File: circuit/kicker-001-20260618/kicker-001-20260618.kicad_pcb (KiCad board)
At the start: 2 copper layers, 71.4 x 62.3 mm, 0 parts

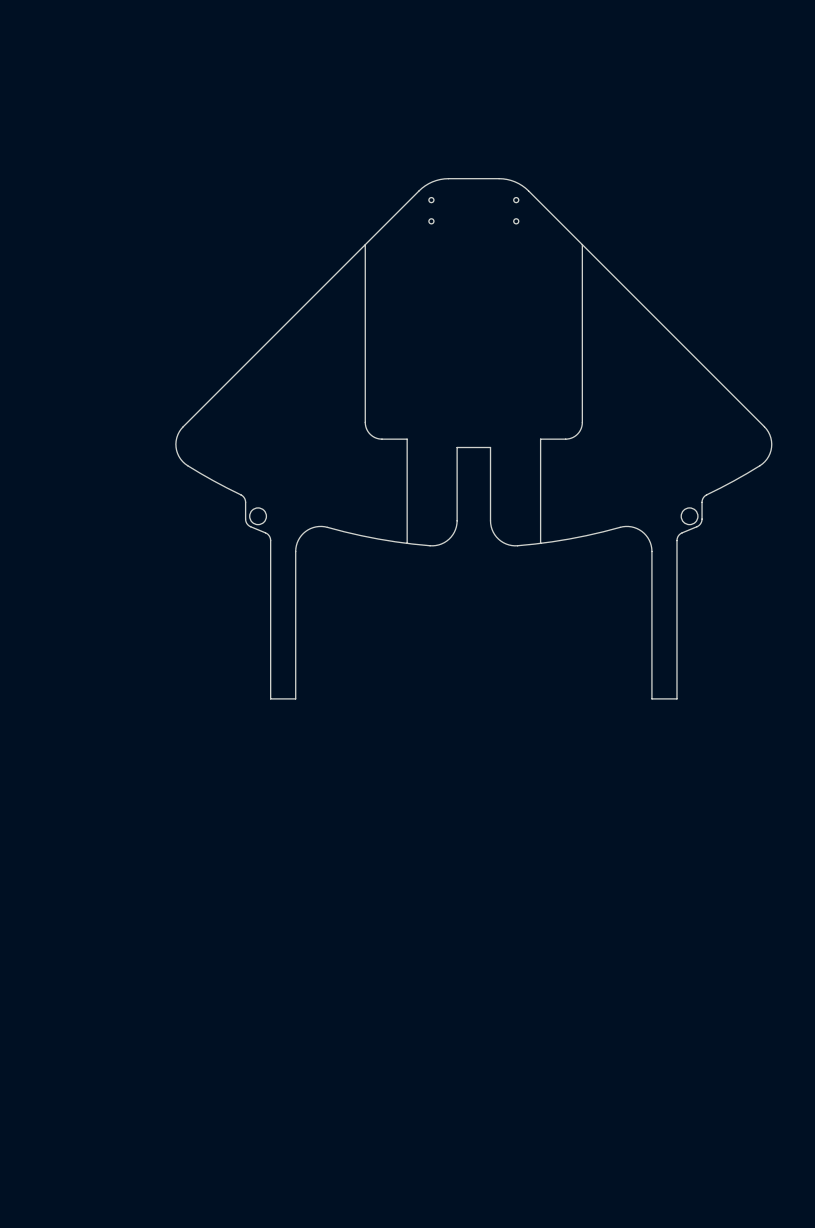
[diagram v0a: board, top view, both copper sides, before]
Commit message: Update キッカー基板のボード図を更新した
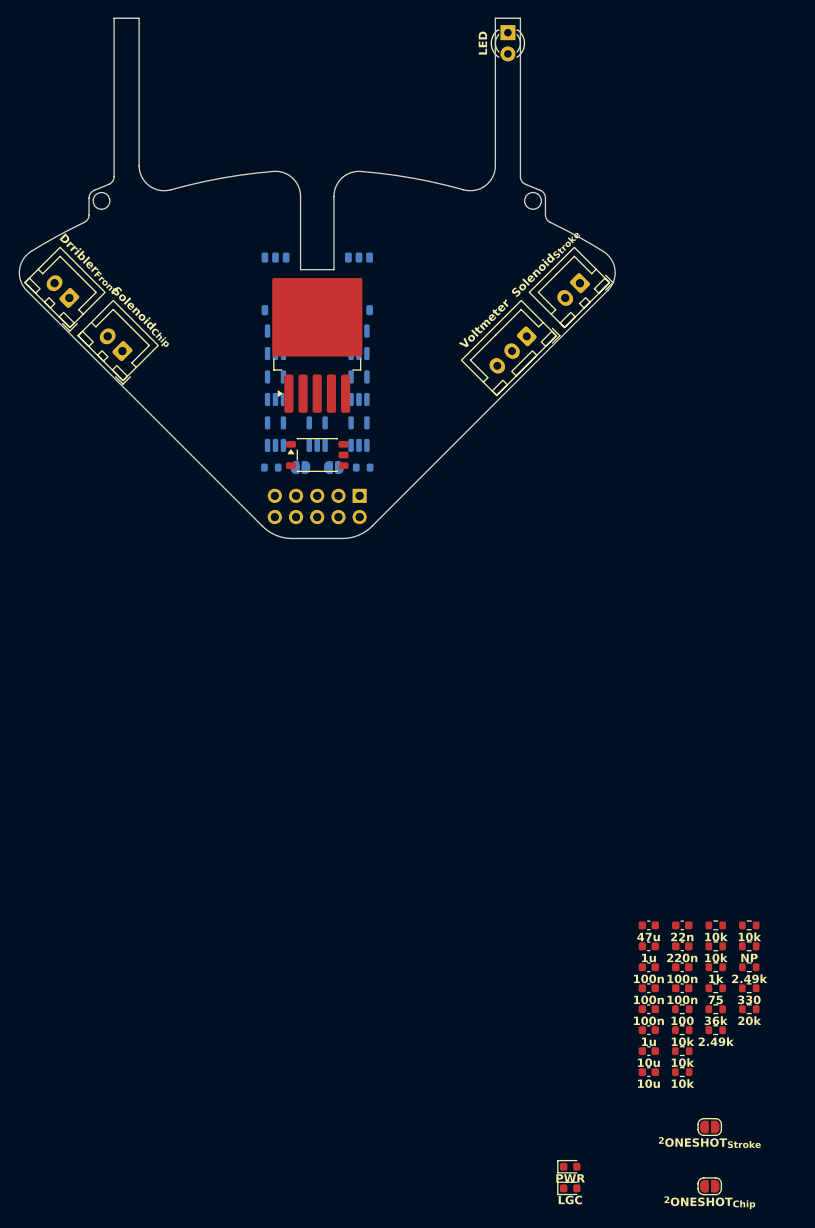
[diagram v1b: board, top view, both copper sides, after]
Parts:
- added C1: 47u, Capacitor_SMD:C_0603_1608Metric, F.Cu at (139.7, 146.3)
- added C10: 220n, Capacitor_SMD:C_0603_1608Metric, F.Cu at (143.7, 148.8)
- added C11: 100n, Capacitor_SMD:C_0603_1608Metric, F.Cu at (143.7, 151.4)
- added C12: 100n, Capacitor_SMD:C_0603_1608Metric, F.Cu at (143.7, 153.9)
- added C2: 1u, Capacitor_SMD:C_0603_1608Metric, F.Cu at (139.7, 148.8)
- added C3: 100n, Capacitor_SMD:C_0603_1608Metric, F.Cu at (139.7, 151.4)
- added C4: 100n, Capacitor_SMD:C_0603_1608Metric, F.Cu at (139.7, 153.9)
- added C5: 100n, Capacitor_SMD:C_0603_1608Metric, F.Cu at (139.7, 156.4)
- added C6: 1u, Capacitor_SMD:C_0603_1608Metric, F.Cu at (139.7, 158.9)
- added C7: 10u, Capacitor_SMD:C_0603_1608Metric, F.Cu at (139.7, 161.4)
- added C8: 10u, Capacitor_SMD:C_0603_1608Metric, F.Cu at (139.7, 163.9)
- added C9: 22n, Capacitor_SMD:C_0603_1608Metric, F.Cu at (143.7, 146.3)
- added D1: LED, LED_THT:LED_D3.0mm, F.Cu at (122.8, 39.4)
- added D3: PWR, LED_SMD:LED_0603_1608Metric, F.Cu at (130.3, 175.2)
- added D4: LGC, LED_SMD:LED_0603_1608Metric, F.Cu at (130.3, 177.8)
- added J1: Solenoid_{Stroke}, Connector_JST:JST_XH_B2B-XH-A_1x02_P2.50mm_Vertical, F.Cu at (131.5, 69.4)
- added J2: Solenoid_{Chip}, Connector_JST:JST_XH_B2B-XH-A_1x02_P2.50mm_Vertical, F.Cu at (76.7, 77.6)
- added J3: Drribler_{Front}, Connector_JST:JST_XH_B2B-XH-A_1x02_P2.50mm_Vertical, F.Cu at (70.3, 71.2)
- added J4: Conn_Relay, Connector_PinSocket_2.54mm:PinSocket_2x05_P2.54mm_Vertical, B.Cu at (105.1, 94.9)
- added J5: Voltmeter, Connector_JST:JST_XH_B3B-XH-A_1x03_P2.50mm_Vertical, F.Cu at (125.1, 75.8)
- added JP1: ^{1}ONESHOT_{Stroke}, Jumper:SolderJumper-2_P1.3mm_Open_RoundedPad1.0x1.5mm, B.Cu at (98.0, 91.5)
- added JP2: ^{2}ONESHOT_{Stroke}, Jumper:SolderJumper-2_P1.3mm_Open_RoundedPad1.0x1.5mm, F.Cu at (147.0, 170.5)
- added JP3: ^{1}ONESHOT_{Chip}, Jumper:SolderJumper-2_P1.3mm_Open_RoundedPad1.0x1.5mm, B.Cu at (102.0, 91.5)
- added JP4: ^{2}ONESHOT_{Chip}, Jumper:SolderJumper-2_P1.3mm_Open_RoundedPad1.0x1.5mm, F.Cu at (147.0, 177.6)
- added R1: 100, Resistor_SMD:R_0603_1608Metric, F.Cu at (143.7, 156.4)
- added R10: 2.49k, Resistor_SMD:R_0603_1608Metric, F.Cu at (147.7, 158.9)
- added R11: 100k, Resistor_SMD:R_0603_1608Metric, B.Cu at (94.5, 91.5)
- added R12: 100k, Resistor_SMD:R_0603_1608Metric, B.Cu at (105.5, 91.5)
- added R13: 10k, Resistor_SMD:R_0603_1608Metric, F.Cu at (151.7, 146.3)
- added R14: NP, Resistor_SMD:R_0603_1608Metric, F.Cu at (151.7, 148.8)
- added R15: 2.49k, Resistor_SMD:R_0603_1608Metric, F.Cu at (151.7, 151.4)
- added R16: 330, Resistor_SMD:R_0603_1608Metric, F.Cu at (151.7, 153.9)
- added R17: 20k, Resistor_SMD:R_0603_1608Metric, F.Cu at (151.7, 156.4)
- added R2: 10k, Resistor_SMD:R_0603_1608Metric, F.Cu at (143.7, 158.9)
- added R3: 10k, Resistor_SMD:R_0603_1608Metric, F.Cu at (143.7, 161.4)
- added R4: 10k, Resistor_SMD:R_0603_1608Metric, F.Cu at (143.7, 163.9)
- added R5: 10k, Resistor_SMD:R_0603_1608Metric, F.Cu at (147.7, 146.3)
- added R6: 10k, Resistor_SMD:R_0603_1608Metric, F.Cu at (147.7, 148.8)
- added R7: 1k, Resistor_SMD:R_0603_1608Metric, F.Cu at (147.7, 151.4)
- added R8: 75, Resistor_SMD:R_0603_1608Metric, F.Cu at (147.7, 153.9)
- added R9: 36k, Resistor_SMD:R_0603_1608Metric, F.Cu at (147.7, 156.4)
- added U1: 74AHC1G04, Package_TO_SOT_SMD:SOT-23-5_HandSoldering, B.Cu at (100.0, 87.5)
- added U10: TLP2361, Package_SO:SO-5-6_4.55x3.7mm_P1.27mm, B.Cu at (105.0, 69.5)
- added U11: 74AHC1G08, Package_TO_SOT_SMD:SOT-23-5_HandSoldering, B.Cu at (95.0, 82.0)
- added U12: 74AHC1G08, Package_TO_SOT_SMD:SOT-23-5_HandSoldering, B.Cu at (105.0, 82.0)
- added U2: TLP2361, Package_SO:SO-5-6_4.55x3.7mm_P1.27mm, F.Cu at (100.0, 90.0)
- added U3: ~, Package_TO_SOT_SMD:TO-263-5_TabPin3, F.Cu at (100.0, 75.0)
- added U4: 74AHC1G04, Package_TO_SOT_SMD:SOT-23-5_HandSoldering, B.Cu at (95.0, 76.5)
- added U5: 74AHC1G04, Package_TO_SOT_SMD:SOT-23-5_HandSoldering, B.Cu at (105.0, 76.5)
- added U7: 74AHC1G04, Package_TO_SOT_SMD:SOT-23-5_HandSoldering, B.Cu at (95.0, 87.5)
- added U8: 74AHC1G04, Package_TO_SOT_SMD:SOT-23-5_HandSoldering, B.Cu at (105.0, 87.5)
- added U9: TLP2361, Package_SO:SO-5-6_4.55x3.7mm_P1.27mm, B.Cu at (95.0, 69.5)
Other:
- outline, holes or cut-outs redrawn

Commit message: Update キッカー基板のcommit残り
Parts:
- removed D3: PWR, LED_SMD:LED_0603_1608Metric
- removed D4: LGC, LED_SMD:LED_0603_1608Metric
- removed R15: 2.49k, Resistor_SMD:R_0603_1608Metric
- removed R16: 330, Resistor_SMD:R_0603_1608Metric
- added D2: D2, @Thrive_footprint_kicker:CUHS20F60, F.Cu at (100.0, 70.5)
- added Q1: BSS138, Package_TO_SOT_SMD:TSOT-23, B.Cu at (103.9, 81.5)
- added Q2: TJ15S06M3L, Package_TO_SOT_SMD:TO-252-2, B.Cu at (99.0, 75.3)
- added Q3: Q_Photo_CE, @Thrive_footprint_kicker:NJL7502L, F.Cu at (125.8, 44.2)
- added Q4: MTB010N06RJ3, Package_TO_SOT_SMD:TO-252-2, F.Cu at (115.5, 84.6)
- added Q5: MTB010N06RJ3, Package_TO_SOT_SMD:TO-252-2, F.Cu at (82.7, 82.8)
- added U6: DRV8874, Package_SO:HTSSOP-16-1EP_4.4x5mm_P0.65mm_EP3.4x5mm_Mask2.66x2.46mm, F.Cu at (79.3, 66.8)
- C1: value 47u -> 47μ; moved to B.Cu
- C10, C11, C12, C3, C4, C5, C9, R1, R10, R13, R14, R17, R2, R3, R4, R5, R6, R7, R8, R9, U2: moved to B.Cu
- C2, C6: value 1u -> 1μ; moved to B.Cu
- C7, C8: value 10u -> 10μ; moved to B.Cu
- JP1: value ^{1}ONESHOT_{Stroke} -> _{ON}; moved to F.Cu
- JP2: value ^{2}ONESHOT_{Stroke} -> _{OFF}
- JP3: value ^{1}ONESHOT_{Chip} -> _{ON}; moved to F.Cu
- JP4: value ^{2}ONESHOT_{Chip} -> _{OFF}
- U1: value 74AHC1G04 -> NOT
- U10, U9: moved to F.Cu
- U11, U12: value 74AHC1G08 -> AND; moved to F.Cu
- U3: value ~ -> XL6009E1
- U4, U5, U7, U8: value 74AHC1G04 -> NOT; moved to F.Cu
- moved R8 127.5 mm to (74.2, 49.8), turned to -90 degrees
- moved R17 121.3 mm to (73.9, 63.4), turned to -135 degrees
- moved R10 119.0 mm to (75.1, 64.6), turned to 45 degrees
- moved R4 115.6 mm to (125.8, 49.8), turned to -90 degrees
- moved R14 114.1 mm to (77.4, 62.3), turned to 45 degrees
- moved R13 113.9 mm to (76.2, 61.1), turned to -135 degrees
- moved JP4 100.7 mm to (94.9, 91.4), turned to 90 degrees
- moved C6 98.3 mm to (96.8, 70.5), turned to 180 degrees
- moved R9 98.3 mm to (100.0, 70.5), turned to 180 degrees
- moved C10 97.9 mm to (82.5, 72.4), turned to -135 degrees
- moved C8 96.5 mm to (92.0, 80.0), turned to -90 degrees
- moved C9 96.4 mm to (85.0, 69.9), turned to -135 degrees
- moved C12 94.9 mm to (86.5, 78.1), turned to 180 degrees
- moved R7 92.3 mm to (103.2, 70.5)
- moved JP2 89.5 mm to (105.1, 91.4), turned to 90 degrees
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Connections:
- D1 pad 1: GND -> Net-(D1-A)
- D1 pad 2: Net-(D1-A) -> GND
- J2 pad 1: +48V -> NMOS^{D}_{BOOST-Chip}
- J2 pad 2: NMOS^{D}_{BOOST-Chip} -> +48V
- J3 pad 1: OUT1_{Dribbler-Front} -> OUT2_{Dribbler-Front}
- J3 pad 2: OUT2_{Dribbler-Front} -> OUT1_{Dribbler-Front}
- J4 pad 1: VCC -> GND
- J4 pad 2: Kick_{Stroke} -> EN_{BOOST}
- J4 pad 3: Kick_{Chip} -> EN_{Dribbler-Front}
- J4 pad 4: EN_{BOOST} -> Kick_{Chip}
- J4 pad 5: GND -> PH_{Dribbler-Front}
- J4 pad 6: GND -> VCC
- J4 pad 8: PH_{Dribbler-Front} -> Kick_{Stroke}
- J4 pad 9: EN_{Dribbler-Front} -> GND
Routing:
- net +3.3V: track 0.00 -> 169.1 mm, vias 0 -> 11
- net +48V: track 0.00 -> 73.3 mm, vias 0 -> 1
- net BallCatch_{Front}: track 0.00 -> 69.4 mm
- net PH_{Dribbler-Front}: track 0.00 -> 60.6 mm, vias 0 -> 1
- net EN_{Dribbler-Front}: track 0.00 -> 58.4 mm, vias 0 -> 2
- net VCC: track 0.00 -> 49.5 mm, vias 0 -> 1
- net Kick_{Chip}: track 0.00 -> 27.1 mm
- net ^{SAFE}VCC: track 0.00 -> 23.8 mm, vias 0 -> 1
- net ^{ONESHOT}Kick_{Chip}: track 0.00 -> 22.9 mm, vias 0 -> 2
- net ^{ONESHOT}Kick_{Stroke}: track 0.00 -> 22.8 mm, vias 0 -> 2
- net Kick_{Stroke}: track 0.00 -> 22.5 mm, vias 0 -> 2
- net Net-(U3-FB): track 0.00 -> 21.4 mm, vias 0 -> 1
- net Net-(Q1-D): track 0.00 -> 20.0 mm
- net Net-(D2-A): track 0.00 -> 14.9 mm
- net OUT2_{Dribbler-Front}: track 0.00 -> 14.3 mm
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- added copper zone on B.Cu, net GND
- added copper zone on F.Cu, net GND
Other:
- board size 71.4 x 62.3 mm -> 71.4 x 59.3 mm
- board text added: "Chip"
- board text added: "Stroke"

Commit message: Update キッカー基板のボード図完成
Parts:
- removed J5: Voltmeter, Connector_JST:JST_XH_B3B-XH-A_1x03_P2.50mm_Vertical
- added J6: Voltmeter, Connector_JST:JST_XH_B2B-XH-A_1x02_P2.50mm_Vertical, F.Cu at (131.7, 69.5)
- added L1: 33u, @Thrive_footprint_kicker:SRC1317, F.Cu at (120.2, 65.6)
- moved C3 2.60 mm to (113.3, 87.2)
- moved J1 2.60 mm to (125.3, 75.9)
- moved Q4 2.60 mm to (117.5, 82.9)
- moved R5 2.60 mm to (114.7, 85.8)
- moved U10 0.25 mm to (86.7, 75.1)
- moved R4 0.25 mm to (126.1, 49.9)
- moved R6 0.25 mm to (85.8, 85.8)
- moved C5 0.25 mm to (107.3, 90.9)
- moved C6 0.25 mm to (97.0, 70.6)
- moved D2 0.25 mm to (100.2, 70.6)
- moved J4 0.25 mm to (95.1, 97.5)
- moved R7 0.25 mm to (103.5, 70.6)
- moved R9 0.25 mm to (100.2, 70.6)
- moved Q3 0.25 mm to (126.1, 44.3)
- moved JP2 0.25 mm to (105.3, 91.5)
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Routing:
- net Net-(D2-A): track 14.9 -> 40.0 mm, vias 0 -> 1
- net ^{SAFE}VCC: track 23.8 -> 42.2 mm
- net GND: track 12.1 -> 24.9 mm, vias 152 -> 131
- net ^{SAFE}Kick_{Stroke}: track 13.5 -> 11.0 mm
- net BallCatch_{Front}: track 69.4 -> 70.6 mm
- net +48V: track 73.3 -> 74.3 mm

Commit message: Update キッカー基板のボード図最終調整やった
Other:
- board text added: "Kicker-001"

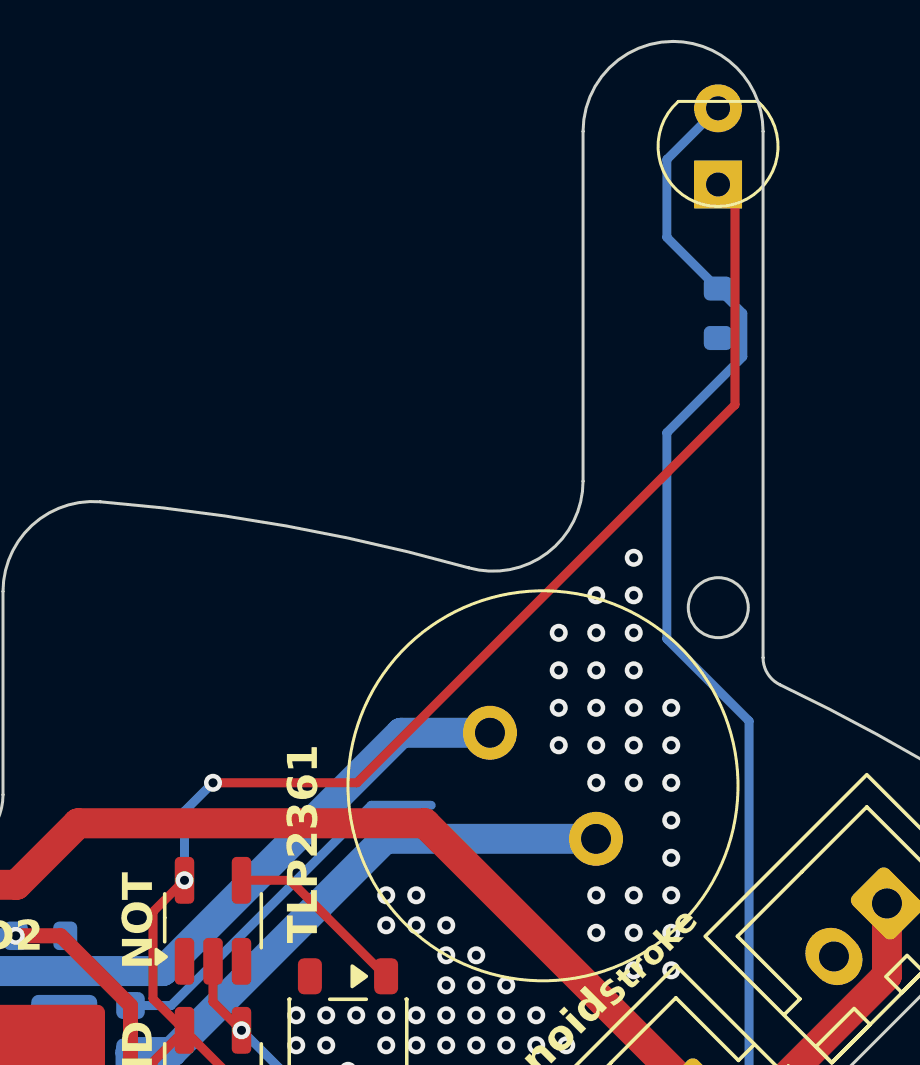
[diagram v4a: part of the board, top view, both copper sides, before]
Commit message: Create メイン基板、MD基板、キッカー基板の発注ファイルを作成
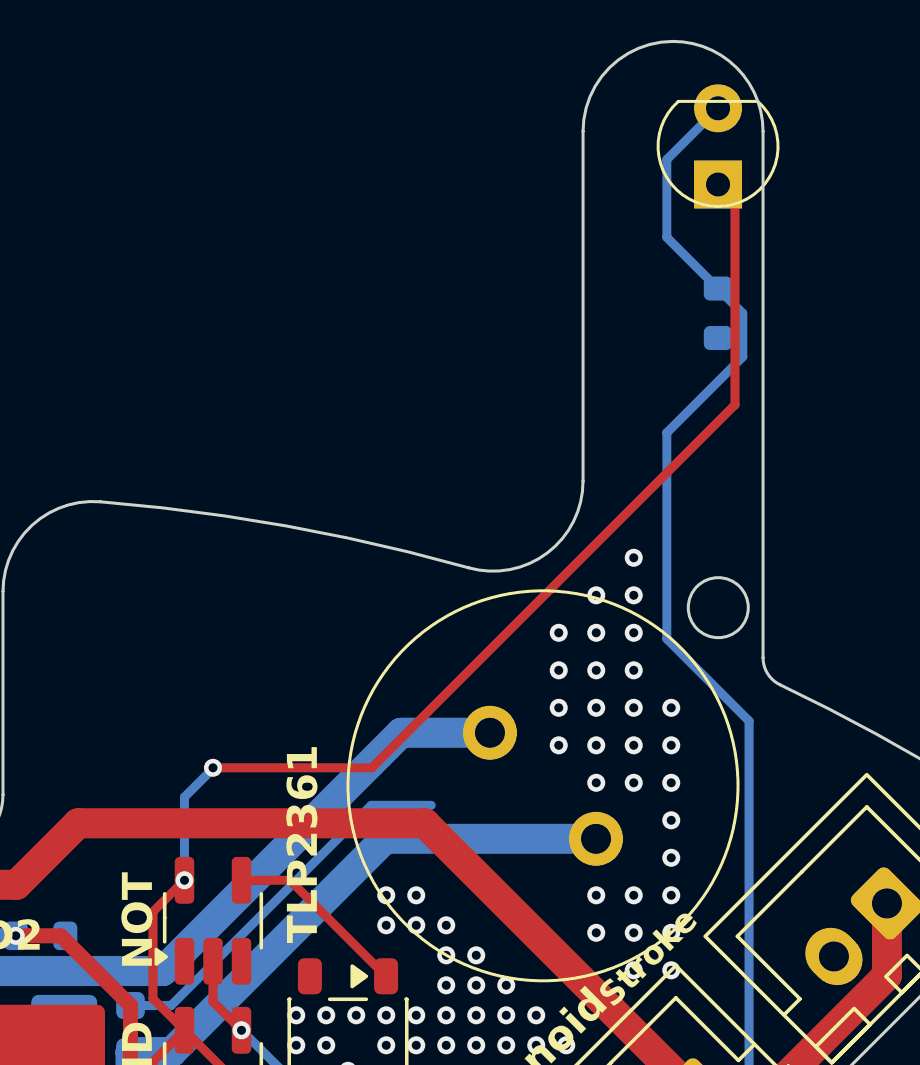
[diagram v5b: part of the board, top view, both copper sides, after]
